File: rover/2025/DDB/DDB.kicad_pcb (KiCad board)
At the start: 4 copper layers, 152.8 x 53.5 mm, 93 parts, among them J1 USB_C_USB4105-GF-A, J2 ETH-RJHSE508104, J3 TerminalBlock, J4 ETH-RJHSE508104, J8 XT30PW-F, SW1 TS09-63-25-WT-160-SMT-TR, SW2 TS09-63-25-WT-160-SMT-TR, U1 ESP32-S3-WROVER, U10 HSS-VN7140ASTR, U11 HSS-VN7140ASTR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

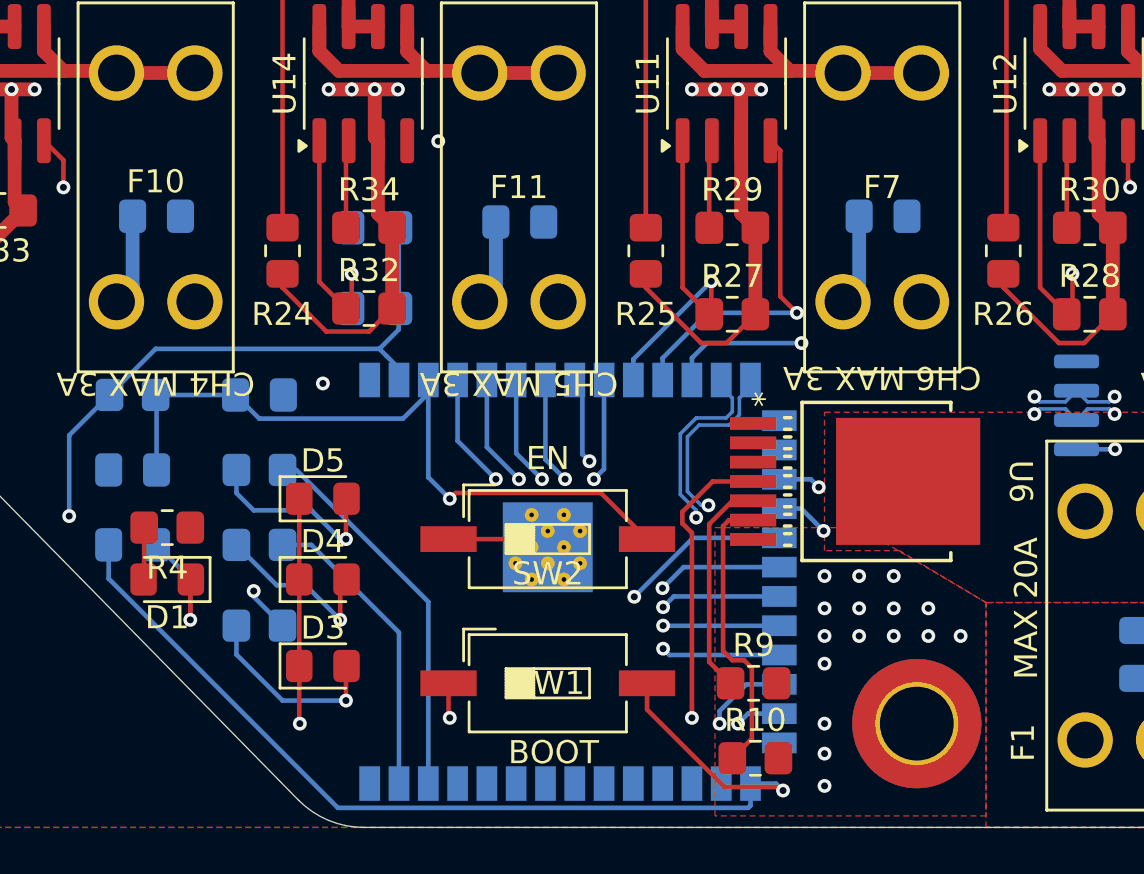
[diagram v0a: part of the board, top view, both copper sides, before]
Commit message: Changed name + silkscreen DDB
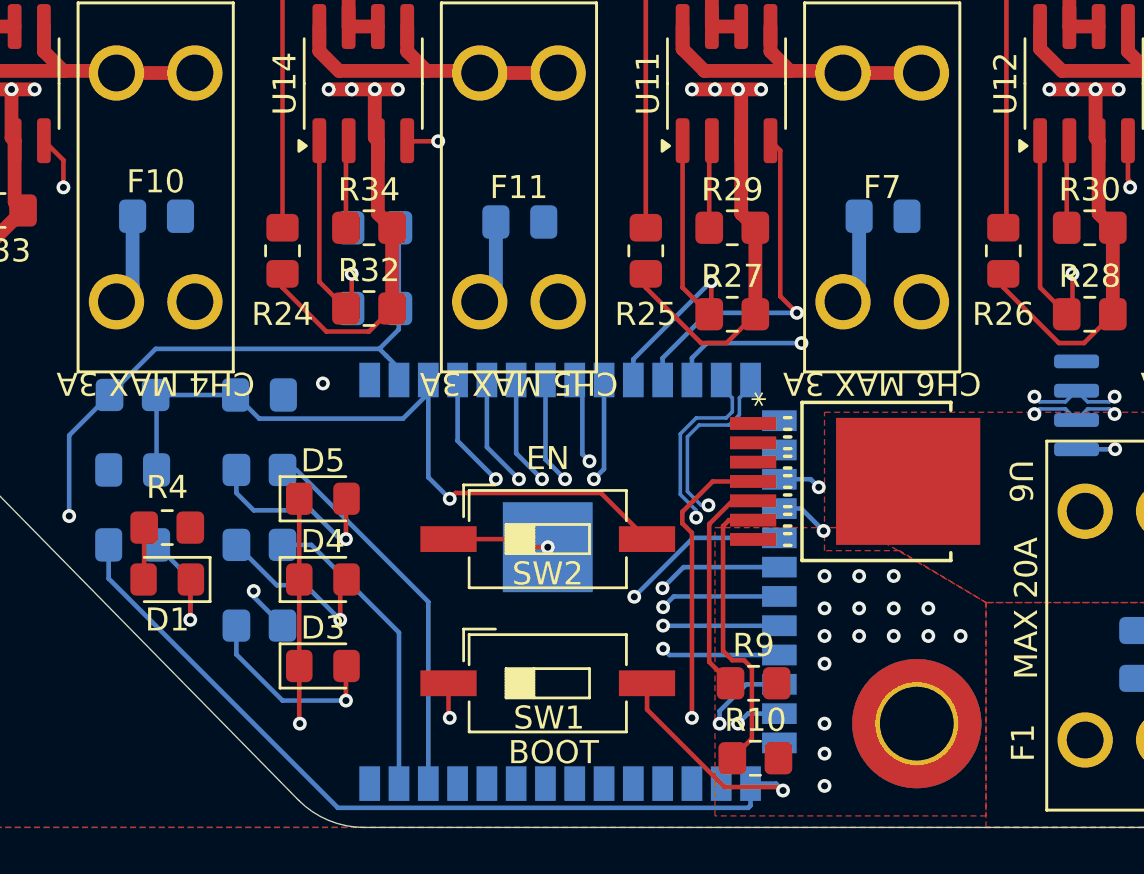
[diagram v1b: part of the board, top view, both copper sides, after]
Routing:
- net GND: track 203.2 -> 204.6 mm, vias 52 -> 53
- net /SIGN_SENSE_24_6: track 23.4 -> 24.7 mm

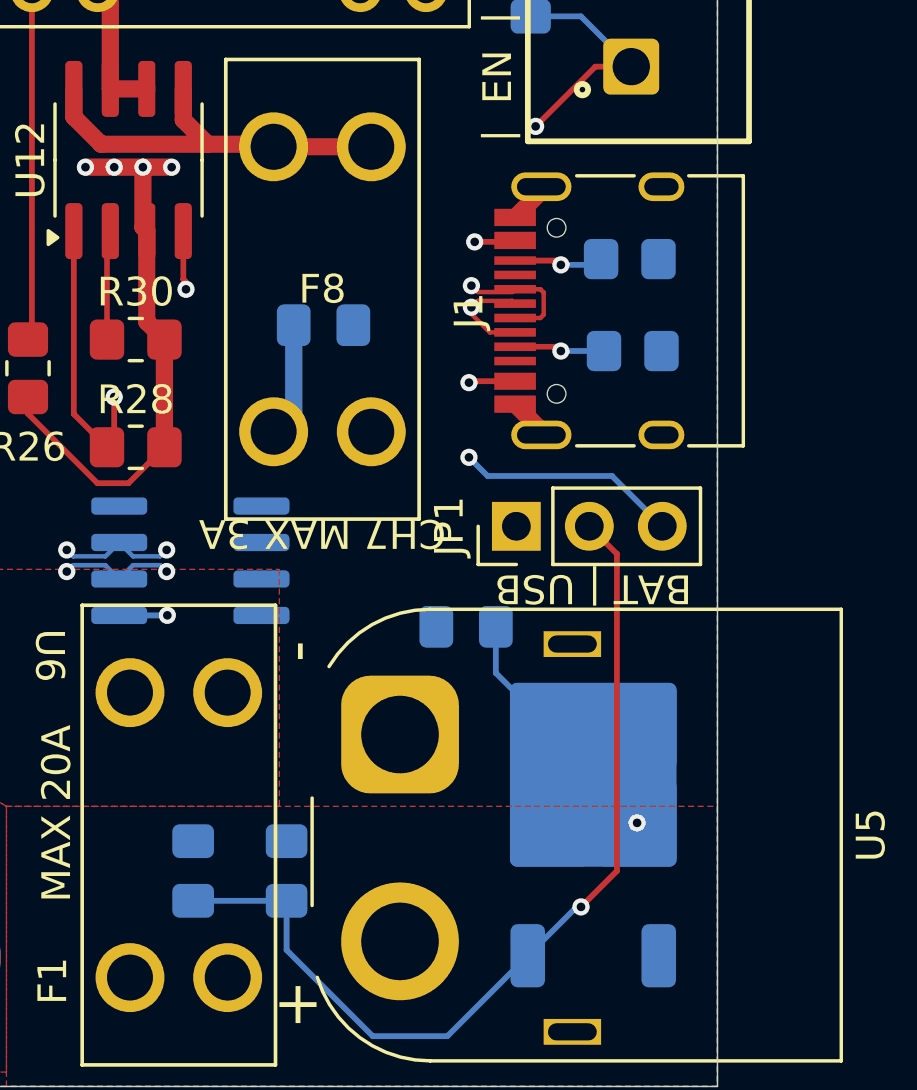
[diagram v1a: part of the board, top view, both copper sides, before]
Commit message: Update sch and pcb for correct link
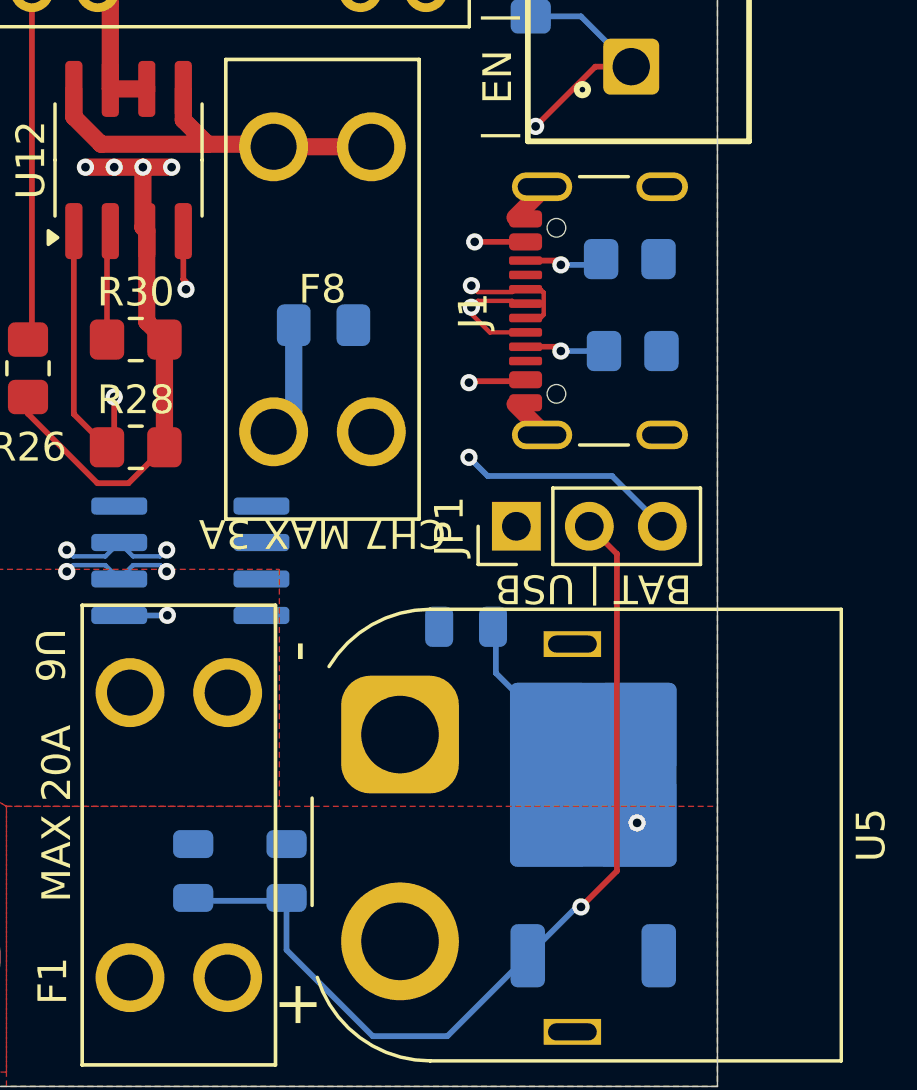
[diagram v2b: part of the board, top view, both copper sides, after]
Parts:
- C10, C9: value 10 uF -> C; footprint Capacitor_SMD:C_0805_2012Metric_Pad1.18x1.45mm_HandSolder -> LED_SMD:LED_0805_2012Metric
- C11, C12, C17, C18, C19, C20, C23, C24, C25: value 22uF -> 10uF
- C8: value 100 nF -> C; footprint Capacitor_SMD:C_0805_2012Metric_Pad1.18x1.45mm_HandSolder -> LED_SMD:LED_0805_2012Metric
- D1, D2: value R -> LED
- D3: value G -> LED
- D4, D5: value B -> LED
- F1: value 20A -> FuseHolder
- F10, F11, F2, F3, F4, F5, F7, F8: value 3A -> FuseHolder
- F6: value 5A -> FuseHolder
- J1: footprint Connector_USB:USB_C_Receptacle_HRO_TYPE-C-31-M-12 -> Connector_USB:USB_C_Receptacle_GCT_USB4105-xx-A_16P_TopMnt_Horizontal
- R10, R11, R12, R13, R14, R15, R16, R19, R20, R27, R28, R29, R30, R31, R32, R33, R34: value 15k -> R
- R17, R18, R21, R22, R23, R24, R25, R26, R35: value 5.1k -> R
- R2, R3: value 5.1k -> k
- R4, R5, R6, R7, R8, R9: value 1k -> R
- U4: value LDO-TLE4284DV33ATMA1 -> LDO-LM7805MPX/NOPB
- U6: value HSS-VN7004SLHTR -> HSS-VN7004SLHTR
